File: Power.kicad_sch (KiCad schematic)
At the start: 9 parts, among them U401 LM4040N-5.0

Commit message: fix: test point changes
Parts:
- removed TP402: GND, TestPoint:TestPoint_THTPad_2.0x2.0mm_Drill1.0mm, symbol Connector:TestPoint
- TP401, TP403: footprint TestPoint:TestPoint_Pad_D1.5mm -> TestPoint:TestPoint_Pad_D1.0mm
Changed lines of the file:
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@@
-	(wire
-		(pts
-			(xy 168.91 96.52) (xy 171.45 96.52)
-		)
-		(stroke
-			(width 0)
-			(type default)
-		)
-	)
 	(wire
 		(pts
@@
 			)
 		)
-		(property "Footprint" "TestPoint:TestPoint_Pad_D1.5mm"
+		(property "Footprint" "TestPoint:TestPoint_Pad_D1.0mm"
 			(at 133.35 93.98 0)
 			(effects
@@
 			)
 		)
-		(property "Datasheet" "~"
+		(property "Datasheet" ""
 			(at 133.35 93.98 0)
 			(effects
@@
 			)
 		)
-		(property "Description" "test point"
+		(property "Description" ""
 			(at 138.43 93.98 0)
 			(effects
@@
 			)
 		)
-		(property "Footprint" "TestPoint:TestPoint_Pad_D1.5mm"
+		(property "Footprint" "TestPoint:TestPoint_Pad_D1.0mm"
 			(at 179.07 80.01 0)
 			(effects
@@
 			)
 		)
-		(property "Datasheet" "~"
+		(property "Datasheet" ""
 			(at 179.07 80.01 0)
 			(effects
@@
 			)
 		)
-		(property "Description" "test point"
+		(property "Description" ""
 			(at 173.99 80.01 0)
 			(effects
@@
 					(unit 1)
 				)
-			)
-		)
-	)
-	(symbol
-		(lib_id "Connector:TestPoint")
-		(at 171.45 96.52 270)
-		(unit 1)
-		(exclude_from_sim no)
-		(in_bom no)
-		(on_board yes)
-		(dnp no)
-		(property "Reference" "TP402"
-			(at 174.625 95.25 90)
-			(effects
-				(font
-					(size 1.27 1.27)
-				)
-				(justify bottom)
-			)
-		)
-		(property "Value" "GND"
-			(at 174.625 97.79 90)
-			(effects
-				(font
-					(size 1.27 1.27)
-				)
-				(justify top)
-			)
-		)
-		(property "Footprint" "TestPoint:TestPoint_THTPad_2.0x2.0mm_Drill1.0mm"
-			(at 171.45 101.6 0)
-			(effects
-				(font
-					(size 1.27 1.27)
-				)
-				(hide yes)
-			)
-		)
-		(property "Datasheet" "~"
-			(at 171.45 101.6 0)
-			(effects
-				(font
-					(size 1.27 1.27)
-				)
-				(hide yes)
-			)
-		)
-		(property "Description" "test point"
-			(at 171.45 96.52 0)
-			(effects
-				(font
-					(size 1.27 1.27)
-				)
-				(hide yes)
-			)
-		)
-		(pin "1"
-		)
-		(instances
-			(project "Input-Protection"
-				(path "/f9e05184-c88b-4a88-ae9c-ab2bdb32be7c/179513e0-5d54-46f9-91b6-4a13d6971432/3dfcbf60-23d2-437c-a8ed-a098d307e8cb"
-					(reference "TP402")
-					(unit 1)
-				)

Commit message: fix: bom improvements & more notes
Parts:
- TP401, TP403: footprint TestPoint:TestPoint_Pad_D1.0mm -> RD-Testpoints:TestPoint_Pad_D1.0mm
- U401: Notes (none) -> VREF = 5.0 V, low temperature coefficient, suitable for pre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
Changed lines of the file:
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@@
+			)
+		)
+		(property "Notes" "VREF = 5.0 V, low temperature coefficient, suitable for precision threshold VREF"
+			(at 168.91 88.9 90)
+			(effects
+				(font
+					(size 1.27 1.27)
+				)
+				(hide yes)
 			)
 		)
@@
 			)
 		)
-		(property "Footprint" "TestPoint:TestPoint_Pad_D1.0mm"
+		(property "Footprint" "RD-Testpoints:TestPoint_Pad_D1.0mm"
 			(at 133.35 93.98 0)
 			(effects
@@
 			)
 		)
-		(property "Footprint" "TestPoint:TestPoint_Pad_D1.0mm"
+		(property "Footprint" "RD-Testpoints:TestPoint_Pad_D1.0mm"
 			(at 179.07 80.01 0)
 			(effects

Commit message: feat: ERC/DRC checks
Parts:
- R401, R402, R403: Manufacturer (none) -> Analog Technologies

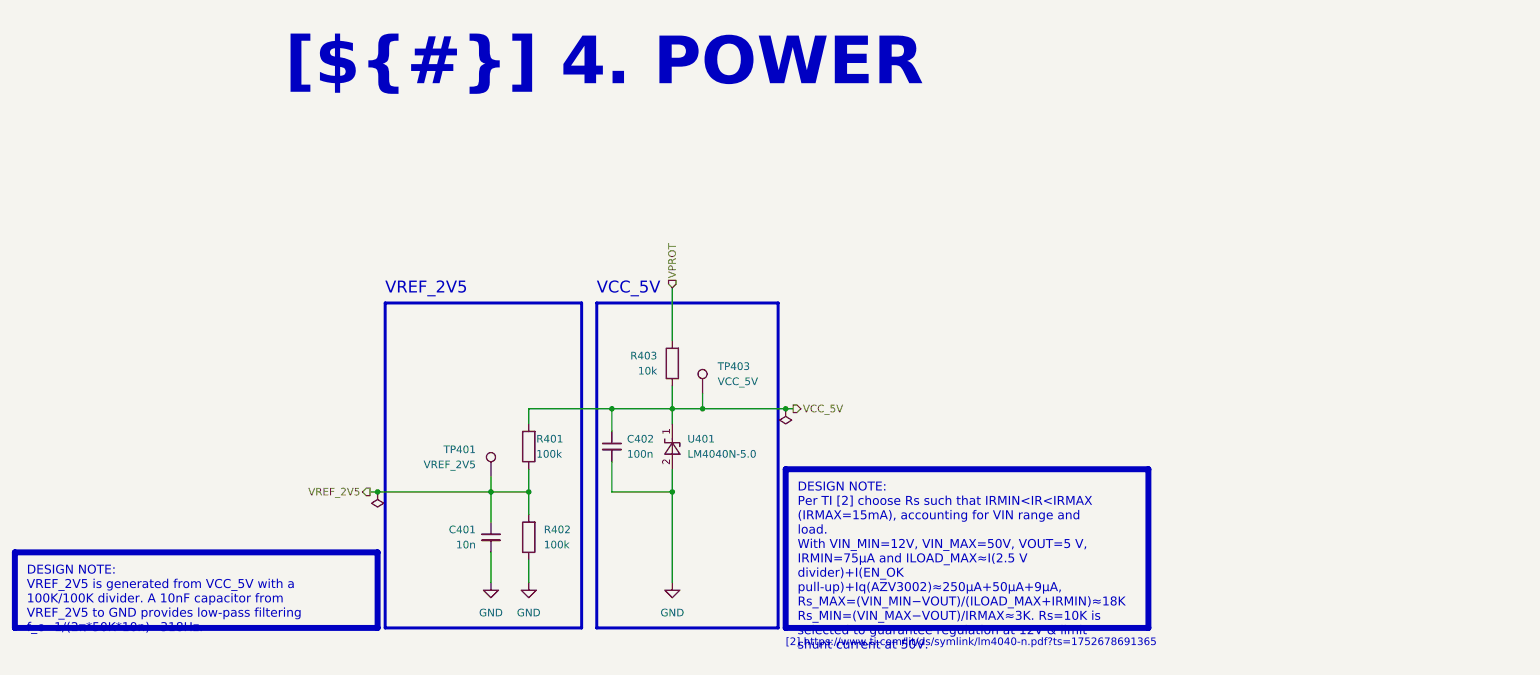
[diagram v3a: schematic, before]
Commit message: feat!: added OC protection, redesigned board from near scratch, size increase
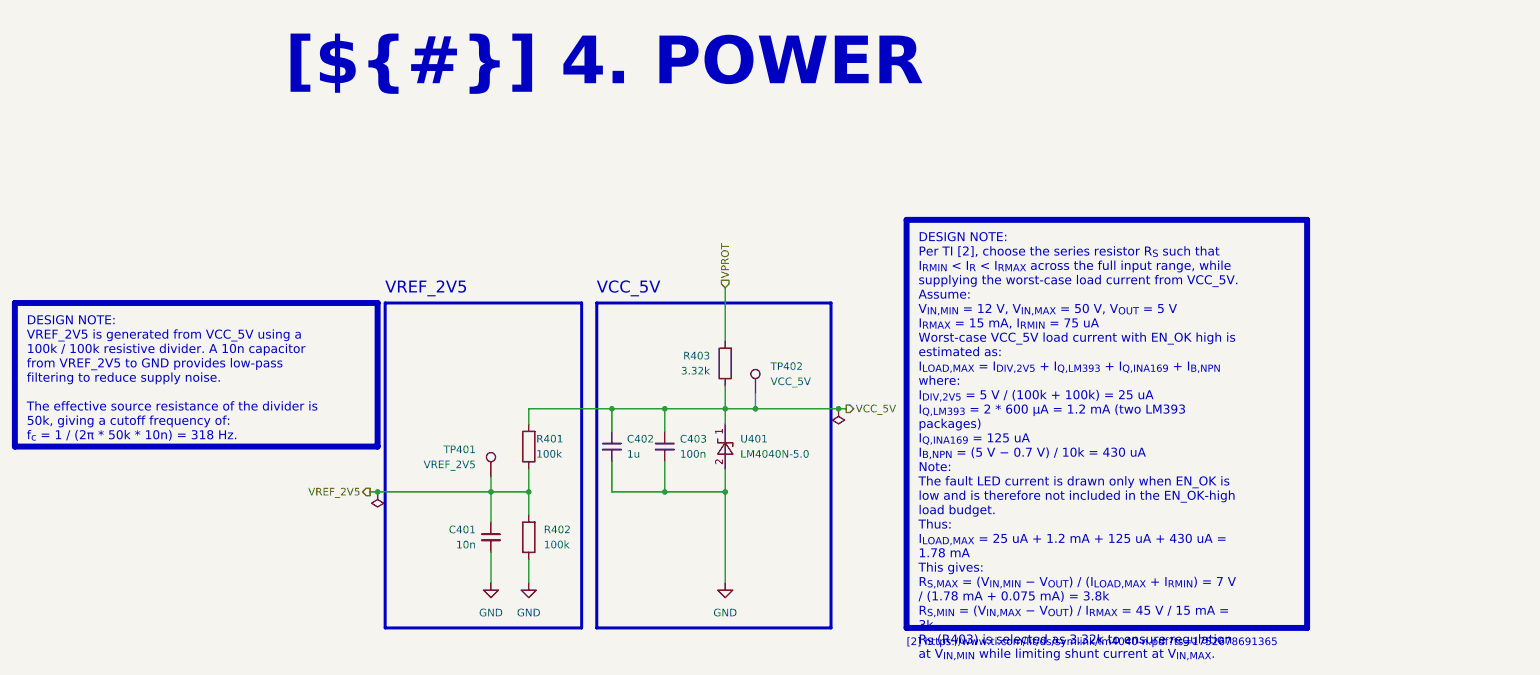
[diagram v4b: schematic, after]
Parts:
- added C402: 1u, Capacitor_SMD:C_0603_1608Metric_Pad1.08x0.95mm_HandSolder, symbol Device:C_Small
- R403: value 10k -> 3.32k
- renumbered C402 to C403, TP403 to TP402
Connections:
- net GND: now also C402.2
- net VCC_5V: now also C402.1
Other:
- moved on the sheet: C403, R403, TP402, U401
